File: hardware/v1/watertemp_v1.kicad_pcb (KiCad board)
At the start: 2 copper layers, 4 parts, among them P1 CONN_01X08, P2 CONN_01X04, P3 CONN_01X07

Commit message: PCB layouting
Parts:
- P1: value CONN_01X08 -> Lora
- P2: value CONN_01X04 -> Sensor
- P3: value CONN_01X07 -> Charger
- moved P3 85.0 mm to (66.0, 84.6), turned to 180 degrees
- moved P2 84.9 mm to (79.2, 154.2), turned to 90 degrees
- moved P1 76.9 mm to (75.7, 80.3), turned to 60 degrees
- moved MBED_SB_1 67.3 mm to (83.3, 121.7)
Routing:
- net GND: track 0.00 -> 119.6 mm, vias 0 -> 2
- net +3V3: track 0.00 -> 96.0 mm
- net Tx: track 0.00 -> 52.8 mm
- net Rx: track 0.00 -> 49.3 mm
- net /SDA: track 0.00 -> 34.0 mm
- net /SCL: track 0.00 -> 29.7 mm
- net +5V: track 0.00 -> 29.3 mm, vias 0 -> 2
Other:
- board outline added: 37.3 x 93.2 mm
- net class Default: clearance 0.2 -> 0.8; trace_width 0.25 -> 1; via_dia 0.6 -> 1.6; via_drill 0.4 -> 0.8
- rule trace_clearance: 0.2 -> 0.8

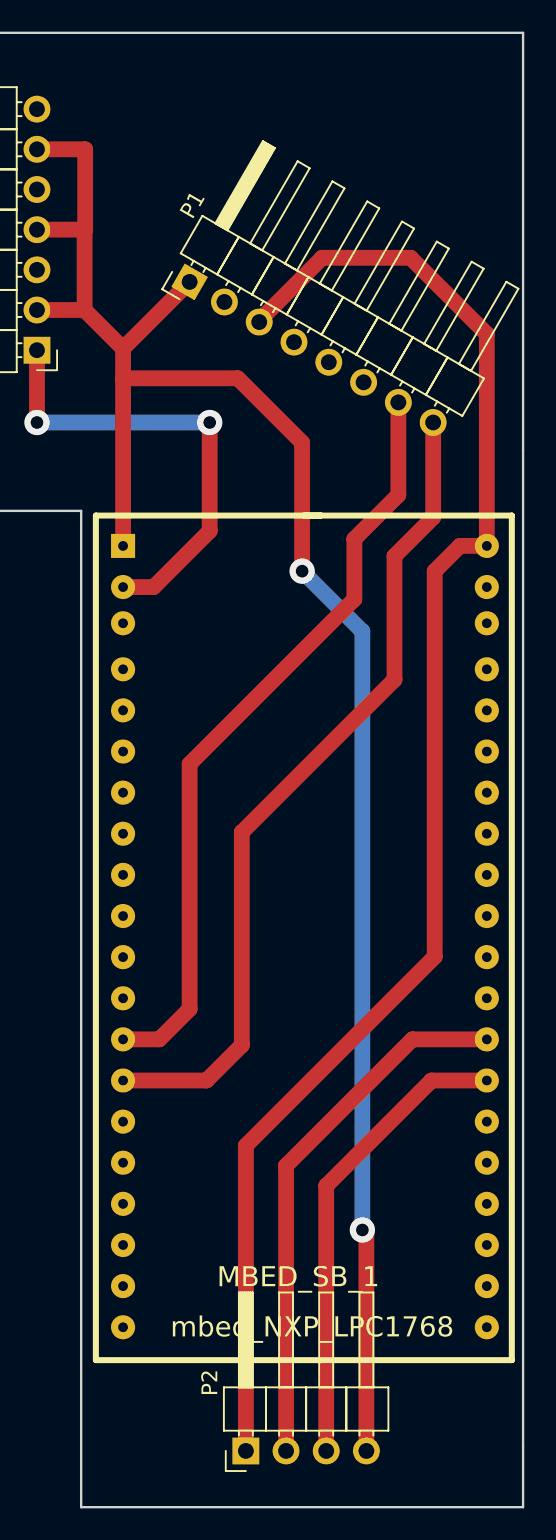
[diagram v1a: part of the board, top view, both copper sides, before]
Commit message: Add text to PCB
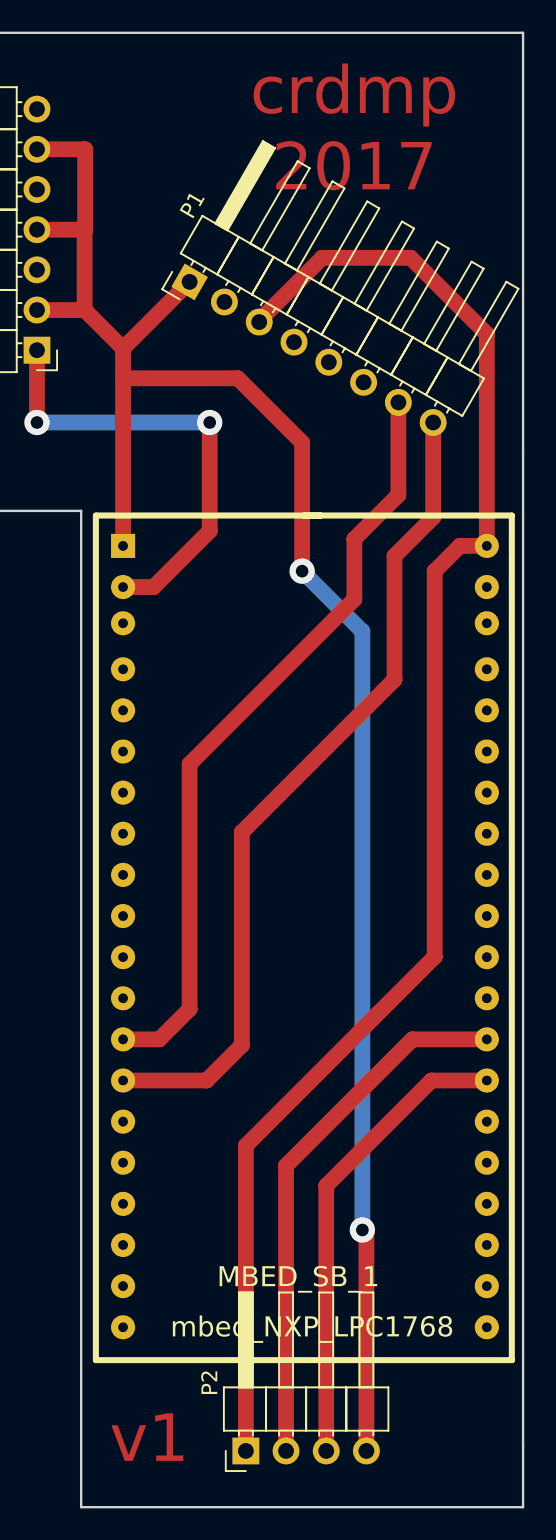
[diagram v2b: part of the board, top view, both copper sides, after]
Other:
- board text added: "crdmp 2017"
- board text added: "v1"
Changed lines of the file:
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@@
     (links 12)
     (no_connects 0)
-    (area 40.536999 11.100999 83.853291 104.469001)
+    (area 55.014999 64.440999 98.331291 157.809001)
     (thickness 1.6)
-    (drawings 8)
+    (drawings 10)
     (tracks 57)
     (zones 0)
@@
     )
   )
+  (gr_text v1 (at 73.152 153.416) (layer F.Cu)
+    (effects (font (size 3 3) (thickness 0.6)))
+  )
+  (gr_text "crdmp\n2017" (at 86.106 70.612) (layer F.Cu)
+    (effects (font (size 3 3) (thickness 0.6)))
+  )
   (gr_line (start 96.774 64.516) (end 59.436 64.516) (angle 90) (layer Edge.Cuts) (width 0.15))
